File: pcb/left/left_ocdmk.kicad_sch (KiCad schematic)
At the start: 101 parts, among them J1 Conn_01x02

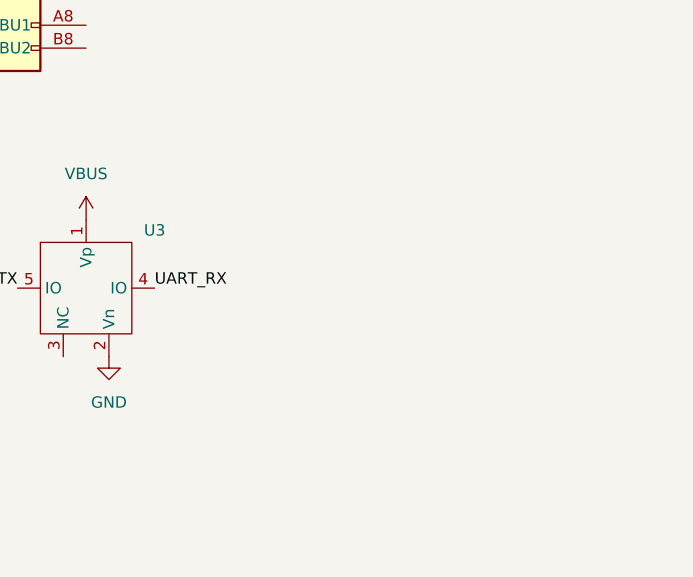
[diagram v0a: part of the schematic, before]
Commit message: Some fixes on PCB
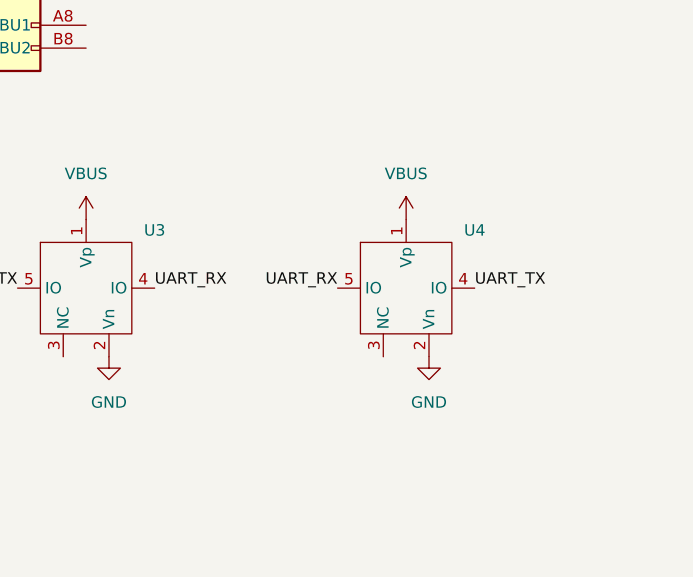
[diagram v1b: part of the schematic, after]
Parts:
- added U4: ~, Package_TO_SOT_SMD:SOT-553, symbol ocdmk:NUP2114
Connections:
- net GND: now also U4.2 (Vn)
- net UART_RX: now also U4.5 (IO)
- net UART_TX: now also U4.4 (IO)
- net VBUS: now also U4.1 (Vp)
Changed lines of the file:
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@@
 		)
 	)
+	(label "UART_RX"
+		(at 283.21 148.59 180)
+		(effects
+			(font
+				(size 1.27 1.27)
+			)
+			(justify right bottom)
+		)
+	)
 	(label "C4"
 		(at 108 35 0)
@@
 		)
 	)
+	(label "UART_TX"
+		(at 298.45 148.59 0)
+		(effects
+			(font
+				(size 1.27 1.27)
+			)
+			(justify left bottom)
+		)
+	)
 	(label "D-"
 		(at 295.91 69.85 90)
@@
 	)
 	(symbol
+		(lib_id "ocdmk:NUP2114")
+		(at 285.75 143.51 0)
+		(unit 1)
+		(exclude_from_sim no)
+		(in_bom yes)
+		(on_board yes)
+		(dnp no)
+		(fields_autoplaced yes)
+		(property "Reference" "U4"
+			(at 298.45 142.1698 0)
+			(effects
+				(font
+					(size 1.27 1.27)
+				)
+			)
+		)
+		(property "Value" "~"
+			(at 298.45 144.7098 0)
+			(effects
+				(font
+					(size 1.27 1.27)
+				)
+			)
+		)
+		(property "Footprint" "Package_TO_SOT_SMD:SOT-553"
+			(at 285.75 143.51 0)
+			(effects
+				(font
+					(size 1.27 1.27)
+				)
+				(hide yes)
+			)
+		)
+		(property "Datasheet" "https://www.onsemi.com/download/data-sheet/pdf/nup2114-d.pdf"
+			(at 285.75 143.51 0)
+			(effects
+				(font
+					(size 1.27 1.27)
+				)
+				(hide yes)
+			)
+		)
+		(property "Description" ""
+			(at 285.75 143.51 0)
+			(effects
+				(font
+					(size 1.27 1.27)
+				)
+				(hide yes)
+			)
+		)
+		(pin "4"
+		)
+		(pin "2"
+		)
+		(pin "3"
+		)
+		(pin "5"
+		)
+		(pin "1"
+		)
+		(instances
+			(project "left_ocdmk"
+				(path "/3ee89390-8d7f-42da-be7f-564d286e2536"
+					(reference "U4")
+					(unit 1)
+				)
+			)
+		)
+	)
+	(symbol
 		(lib_id "Device:LED")
 		(at 137.16 274.32 180)
@@
 	)
 	(symbol
+		(lib_id "power:VBUS")
+		(at 290.83 140.97 0)
+		(unit 1)
+		(exclude_from_sim no)
+		(in_bom yes)
+		(on_board yes)
+		(dnp no)
+		(fields_autoplaced yes)
+		(property "Reference" "#PWR019"
+			(at 290.83 144.78 0)
+			(effects
+				(font
+					(size 1.27 1.27)
+				)
+				(hide yes)
+			)
+		)
+		(property "Value" "VBUS"
+			(at 290.83 135.89 0)
+			(effects
+				(font
+					(size 1.27 1.27)
+				)
+			)
+		)
+		(property "Footprint" ""
+			(at 290.83 140.97 0)
+			(effects
+				(font
+					(size 1.27 1.27)
+				)
+				(hide yes)
+			)
+		)
+		(property "Datasheet" ""
+			(at 290.83 140.97 0)
+			(effects
+				(font
+					(size 1.27 1.27)
+				)
+				(hide yes)
+			)
+		)
+		(property "Description" "Power symbol creates a global label with name \"VBUS\""
+			(at 290.83 140.97 0)
+			(effects
+				(font
+					(size 1.27 1.27)
+				)
+				(hide yes)
+			)
+		)
+		(pin "1"
+		)
+		(instances
+			(project "left_ocdmk"
+				(path "/3ee89390-8d7f-42da-be7f-564d286e2536"
+					(reference "#PWR019")
+					(unit 1)
+				)
+			)
+		)
+	)
+	(symbol
 		(lib_id "Device:LED")
 		(at 120.65 274.32 180)
@@
 					(unit 1)
 				)
+			)
+		)
+	)
+	(symbol
+		(lib_id "power:GND")
+		(at 293.37 156.21 0)
+		(unit 1)
+		(exclude_from_sim no)
+		(in_bom yes)
+		(on_board yes)
+		(dnp no)
+		(fields_autoplaced yes)
+		(property "Reference" "#PWR020"
+			(at 293.37 162.56 0)
+			(effects
+				(font
+					(size 1.27 1.27)
+				)
+				(hide yes)
+			)
+		)
+		(property "Value" "GND"
+			(at 293.37 161.29 0)
+			(effects
+				(font
+					(size 1.27 1.27)
+				)
+			)
+		)
+		(property "Footprint" ""
+			(at 293.37 156.21 0)
+			(effects
+				(font
+					(size 1.27 1.27)
+				)
+				(hide yes)
+			)
+		)
+		(property "Datasheet" ""
+			(at 293.37 156.21 0)
+			(effects
+				(font
+					(size 1.27 1.27)
+				)
+				(hide yes)
+			)
+		)
+		(property "Description" "Power symbol creates a global label with name \"GND\" , ground"
+			(at 293.37 156.21 0)
+			(effects
+				(font
+					(size 1.27 1.27)
+				)
+				(hide yes)
+			)
+		)
+		(pin "1"
+		)
+		(instances
+			(project "left_ocdmk"
+				(path "/3ee89390-8d7f-42da-be7f-564d286e2536"
+					(reference "#PWR020")
+					(unit 1)
+				)
